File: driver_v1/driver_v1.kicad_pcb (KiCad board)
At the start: 4 copper layers, 100 x 66.1 mm, 92 parts, among them J1 PMT, J2 SMA, J4 USB_B, Q1 MMBT2222A, Q2 MMBT2222A, T1 FL2015-9L, U1 ADP1613, U2 OPA314AIDBV, U3 ADA4891-1, U4 TPS7A2045PDBVR

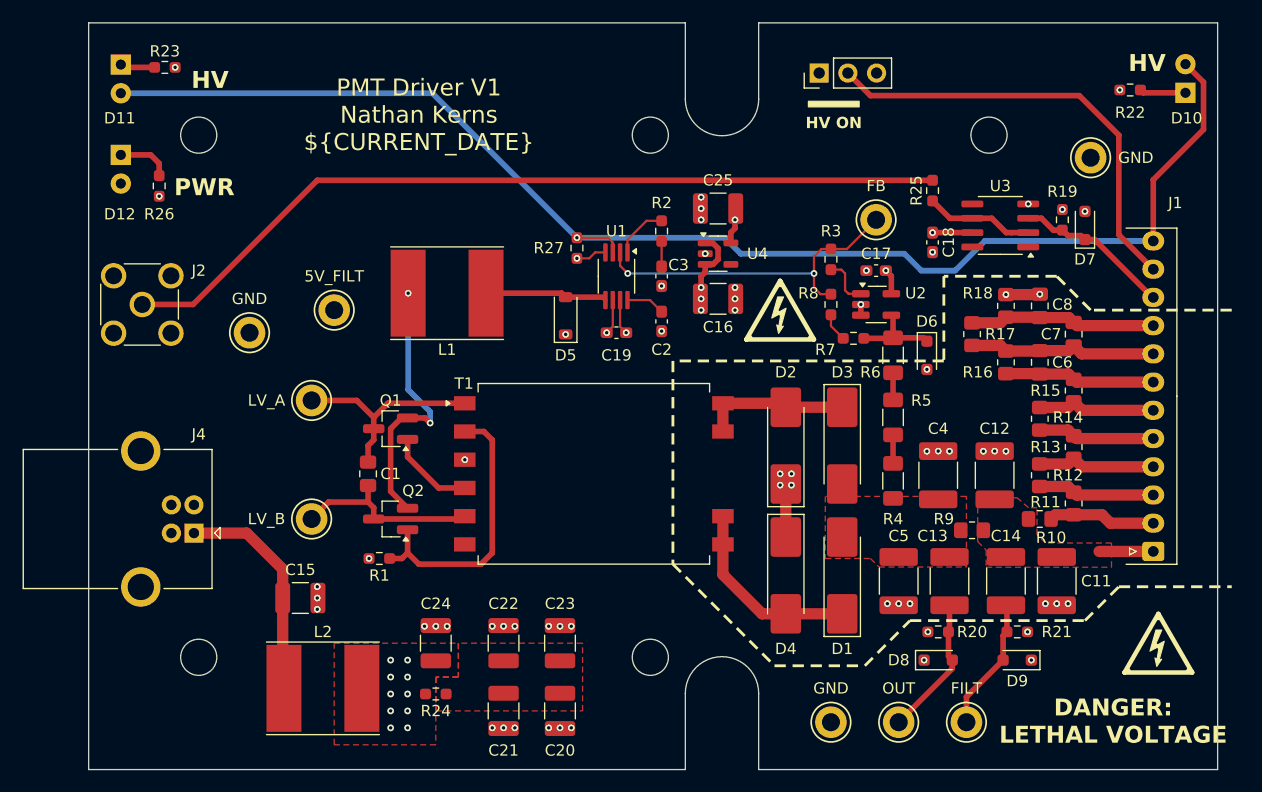
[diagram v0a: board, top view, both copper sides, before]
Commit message: Swap LEDs, update 3D models
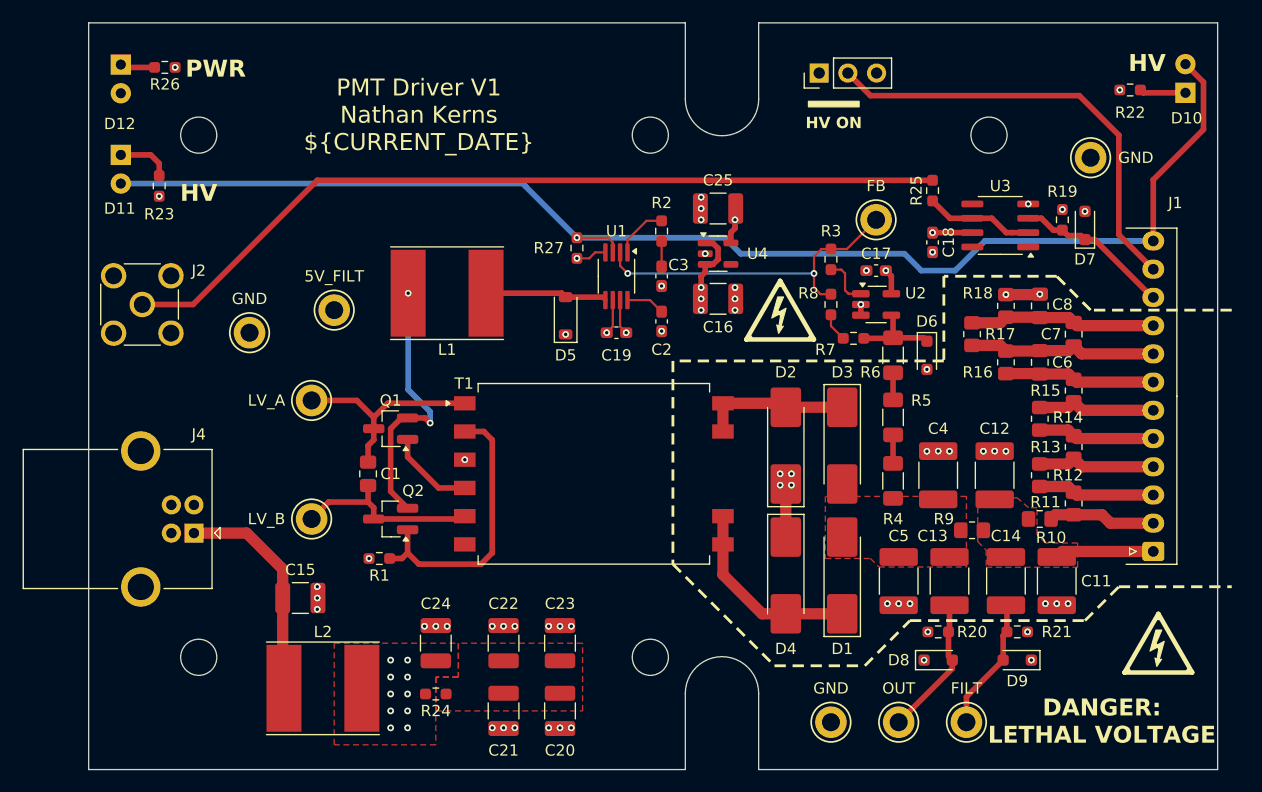
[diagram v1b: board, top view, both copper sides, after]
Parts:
- moved R23 10.5 mm to (71.5, 104.5), turned to -90 degrees
- moved R26 10.5 mm to (72.0, 94.0), turned to 0 degrees
- moved D11 8.00 mm to (68.1, 101.8)
- moved D12 8.00 mm to (68.1, 93.8)
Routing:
- net /FILT: track 4.80 -> 8.75 mm
- net /EN_HV: track 121.4 -> 118.1 mm
- net Net-(D12-K): track 4.80 -> 3.09 mm
- net Net-(D11-K): track 3.09 -> 4.80 mm

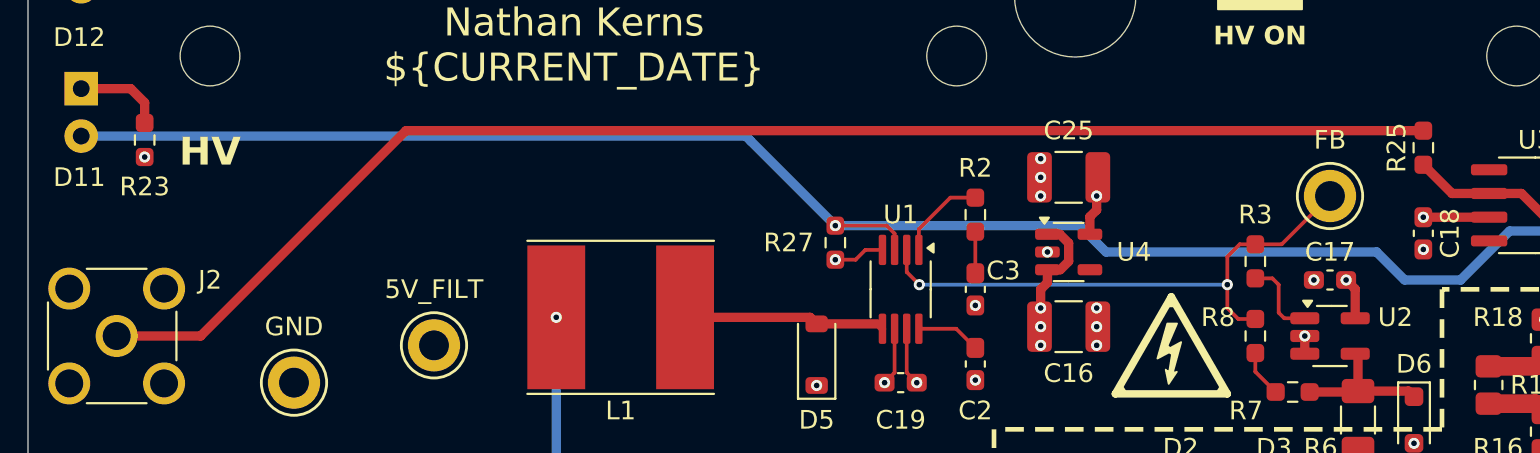
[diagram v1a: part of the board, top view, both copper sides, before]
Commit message: Include screws in BOM, add serial number location
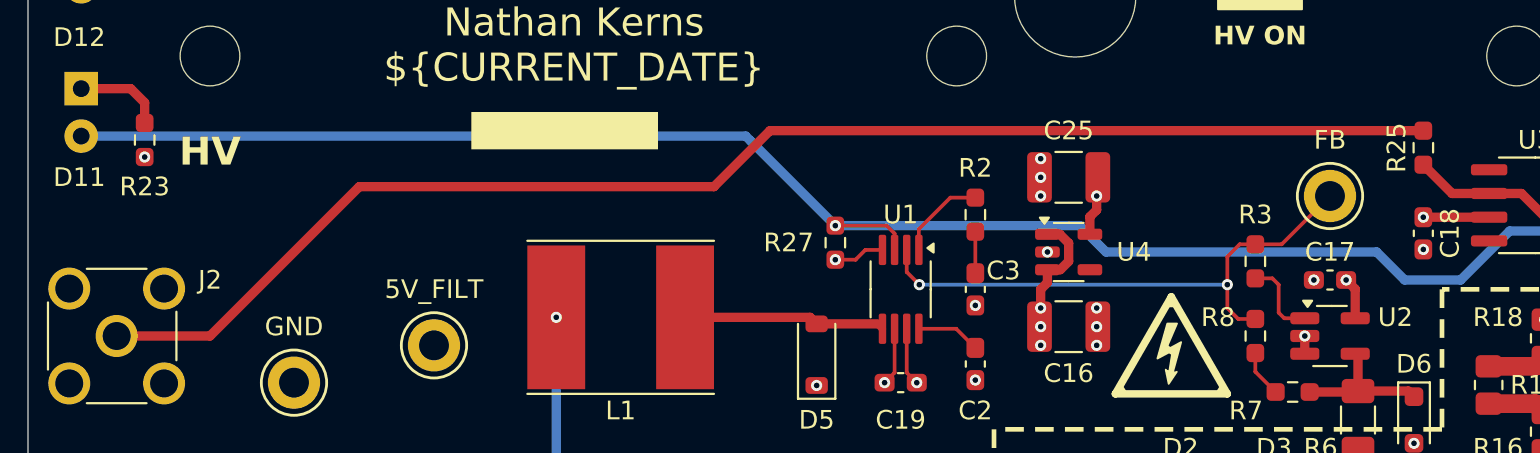
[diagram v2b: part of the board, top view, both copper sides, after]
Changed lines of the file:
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@@
+		(layer "F.SilkS")
+	)
+	(gr_rect
+		(start 89 103)
+		(end 99 105)
+		(stroke
+			(width 0)
+			(type default)
+		)
+		(fill solid)
 		(layer "F.SilkS")
 	)
@@
 	)
 	(segment
-		(start 85.5 104)
+		(start 83 107)
+		(end 102 107)
+		(width 0.5)
+		(layer "F.Cu")
+		(net 27)
+	)
+	(segment
+		(start 75 115)
+		(end 83 107)
+		(width 0.5)
+		(layer "F.Cu")
+		(net 27)
+	)
+	(segment
+		(start 105 104)
 		(end 140 104)
 		(width 0.5)
@@
 	)
 	(segment
-		(start 74.5 115)
-		(end 85.5 104)
+		(start 70 115)
+		(end 75 115)
 		(width 0.5)
 		(layer "F.Cu")
@@
 	)
 	(segment
-		(start 70 115)
-		(end 74.5 115)
-		(width 0.5)
-		(layer "F.Cu")
+		(start 102 107)
+		(end 105 104)
+		(width 0.5)
+		(layer "F.Cu")
